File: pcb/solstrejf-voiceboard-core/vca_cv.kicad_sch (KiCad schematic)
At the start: 0 parts

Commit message: Inital draft of the voice board power supplys and core.
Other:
- title: (none) -> VCA Control Voltage Summing Amplifier
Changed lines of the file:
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@@
 	(generator_version "8.0")
 	(paper "A4")
+	(title_block
+		(title "VCA Control Voltage Summing Amplifier")
+		(date "2024-08-24")
+		(rev "1.0")
+	)
 )

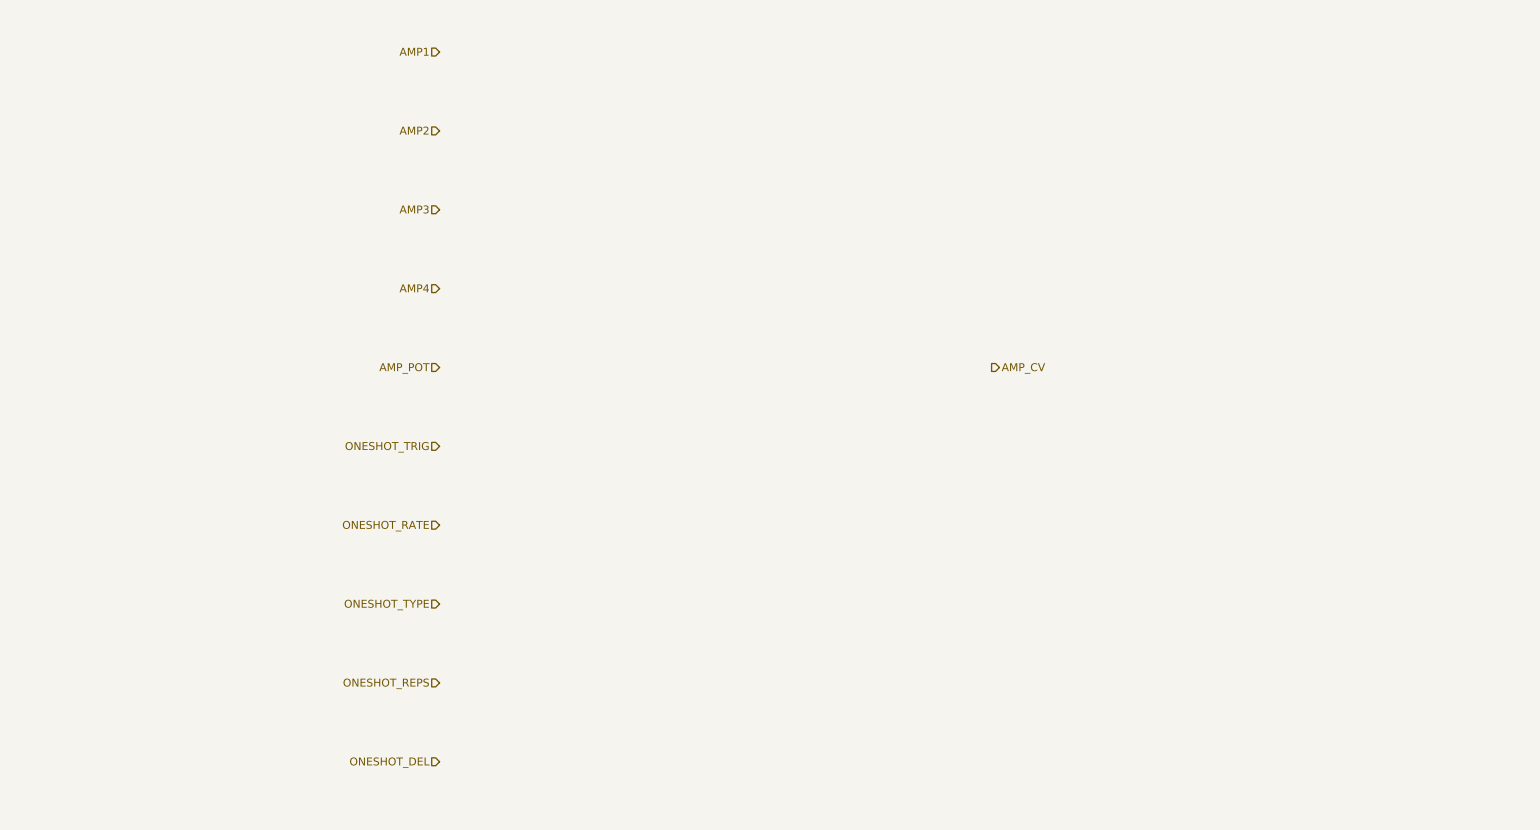
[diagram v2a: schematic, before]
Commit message: created schematic for CV circuits: PAN, VCA, and FREQ. Created a new symbol for the ONESHOT envelope generator
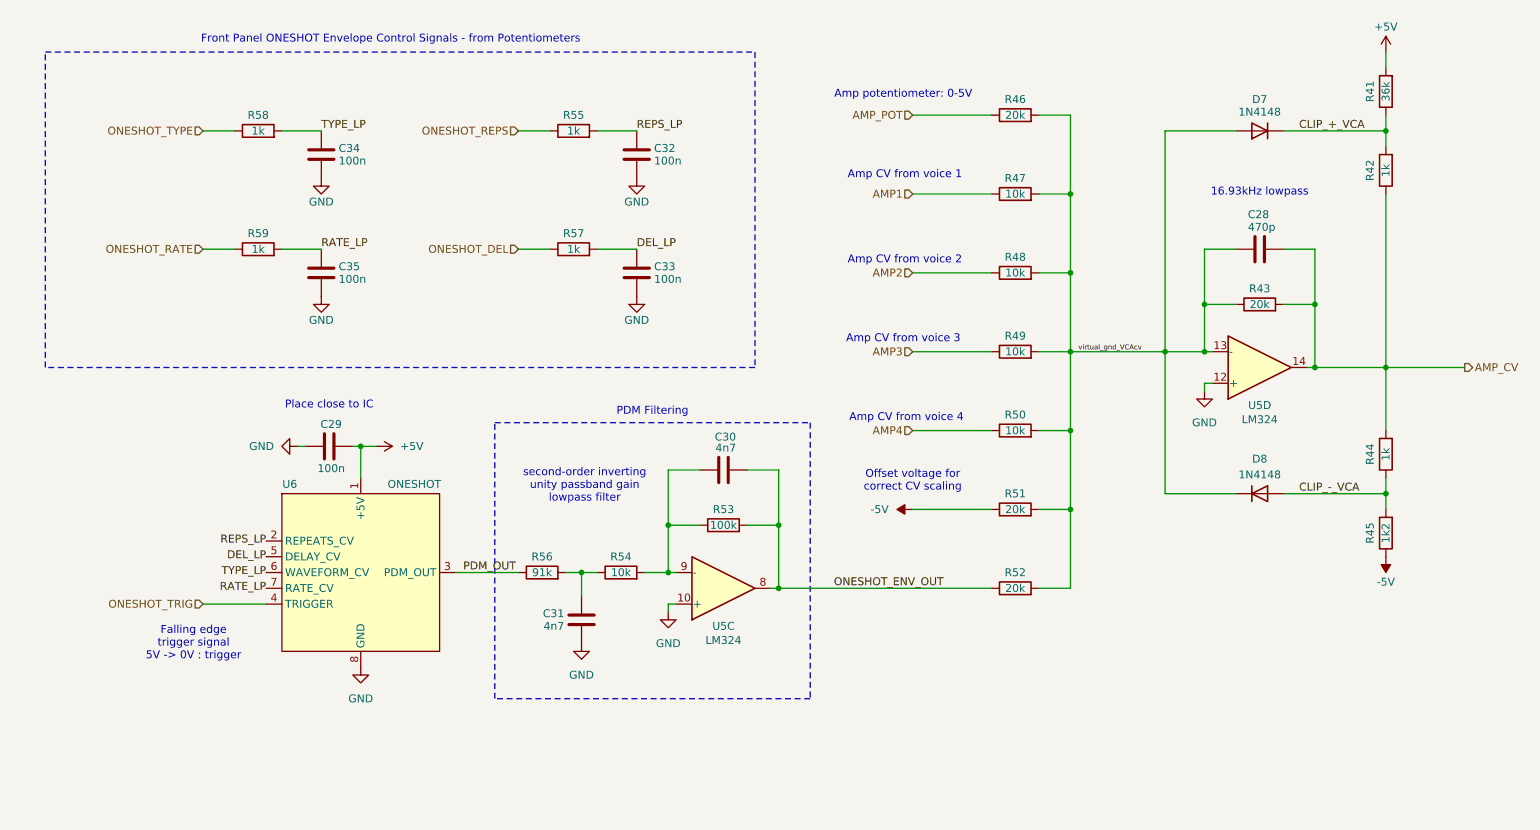
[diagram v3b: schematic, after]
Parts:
- added C28: 470p, Capacitor_THT:C_Disc_D5.0mm_W2.5mm_P5.00mm, symbol Device:C
- added C29, C32, C33, C34, C35: 100n, Capacitor_THT:C_Disc_D5.0mm_W2.5mm_P5.00mm, symbol Device:C
- added C30, C31: 4n7, Capacitor_THT:C_Disc_D5.0mm_W2.5mm_P5.00mm, symbol Device:C
- added D7, D8: 1N4148, Diode_THT:D_DO-35_SOD27_P7.62mm_Horizontal, symbol Diode:1N4148
- added R41: 36k, Resistor_THT:R_Axial_DIN0207_L6.3mm_D2.5mm_P10.16mm_Horizontal, symbol Device:R
- added R42, R44, R55, R57, R58, R59: 1k, Resistor_THT:R_Axial_DIN0207_L6.3mm_D2.5mm_P10.16mm_Horizontal, symbol Device:R
- added R43, R46, R51, R52: 20k, Resistor_THT:R_Axial_DIN0207_L6.3mm_D2.5mm_P10.16mm_Horizontal, symbol Device:R
- added R45: 1k2, Resistor_THT:R_Axial_DIN0207_L6.3mm_D2.5mm_P10.16mm_Horizontal, symbol Device:R
- added R47, R48, R49, R50, R54: 10k, Resistor_THT:R_Axial_DIN0207_L6.3mm_D2.5mm_P10.16mm_Horizontal, symbol Device:R
- added R53: 100k, Resistor_THT:R_Axial_DIN0207_L6.3mm_D2.5mm_P10.16mm_Horizontal, symbol Device:R
- added R56: 91k, Resistor_THT:R_Axial_DIN0207_L6.3mm_D2.5mm_P10.16mm_Horizontal, symbol Device:R
- added U5: LM324, Package_DIP:DIP-14_W7.62mm, symbol Amplifier_Operational:LM324
- added U6: ONESHOT, Package_DIP:DIP-8_W7.62mm_Socket, symbol Kromftronics_Custom:ONSHOT
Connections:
- net AMP1: now also R47.1
- net AMP2: now also R48.1
- net AMP3: now also R49.1
- net AMP4: now also R50.1
- net AMP_CV: now also C28.2, R42.1, R43.2, R44.2, U5.14
- net AMP_POT: now also R46.1
- net ONESHOT_DEL: now also R57.1
- net ONESHOT_RATE: now also R59.1
- net ONESHOT_REPS: now also R55.1
- net ONESHOT_TRIG: now also U6.4 (TRIGGER)
- net ONESHOT_TYPE: now also R58.1
- new net: C31.2, R54.1, R56.2
- new net: C30.1, R53.1, R54.2, U5.9 (-)
- new net +5V: C29.2, R41.2, U6.1 (+5V)
- new net -5V: R45.1, R51.1
- new net CLIP_+_VCA: D7.1 (K), R41.1, R42.2
- new net CLIP_-_VCA: D8.2 (A), R44.1, R45.2
- new net DEL_LP: C33.2, R57.2, U6.5 (DELAY_CV)
- new net GND: C29.1, C31.1, C32.1, C33.1, C34.1, C35.1, U5.10 (+), U5.12 (+), U6.8 (GND)
- new net ONESHOT_ENV_OUT: C30.2, R52.1, R53.2, U5.8
- new net PDM_OUT: R56.1, U6.3 (PDM_OUT)
- new net RATE_LP: C35.2, R59.2, U6.7 (RATE_CV)
- new net REPS_LP: C32.2, R55.2, U6.2 (REPEATS_CV)
- new net TYPE_LP: C34.2, R58.2, U6.6 (WAVEFORM_CV)
- new net virtual_gnd_VCAcv: C28.1, D7.2 (A), D8.1 (K), R43.1, R46.2, R47.2, R48.2, R49.2, R50.2, R51.2, R52.2, U5.13 (-)
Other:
- note added: "16.93kHz lowpass"
- note added: "Amp CV from voice 1"
- note added: "Amp CV from voice 2"
- note added: "Amp CV from voice 3"
- note added: "Amp CV from voice 4"
- note added: "Amp potentiometer: 0-5V"
- note added: "Falling edge trigger signal 5V -> 0V : trigger"
- note added: "Front Panel ONESHOT Envelope Control Signals - from Potentiometers"
- note added: "Offset voltage for correct CV scaling"
- note added: "PDM Filtering"
- note added: "Place close to IC"
- note added: "second-order inverting unity passband gain lowpass filter"

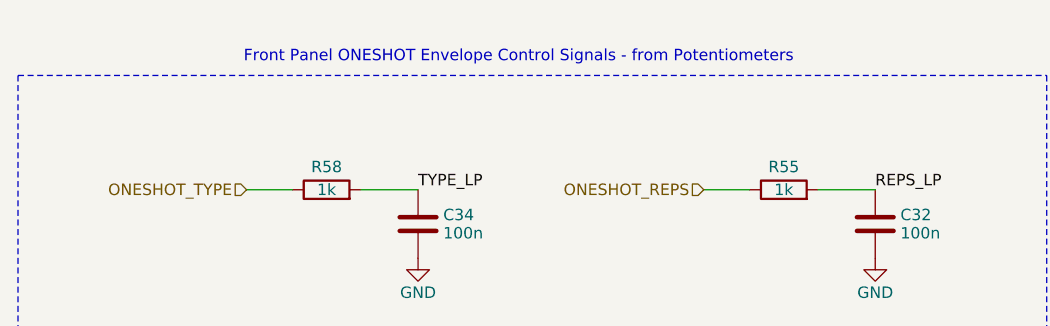
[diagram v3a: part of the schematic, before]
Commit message: created voice board front panel KiCad projects. Made some updates in the Kromftronics KiCad repo.
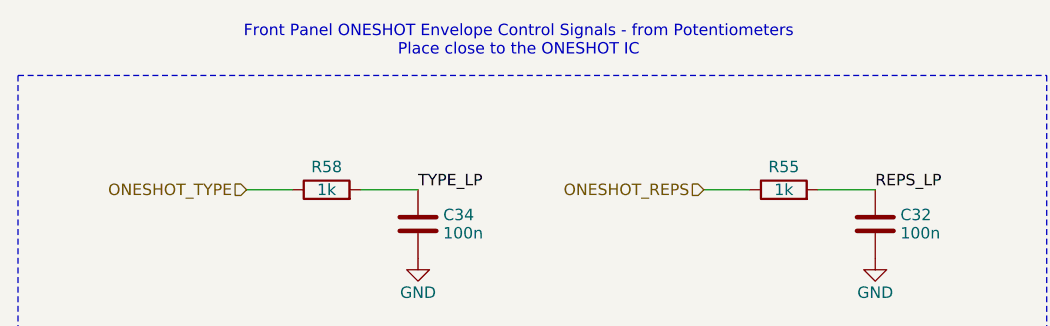
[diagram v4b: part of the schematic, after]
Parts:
- U6: symbol Kromftronics_Custom:ONSHOT -> Kromftronics_Custom:ONESHOT
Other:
- note added: "Front Panel ONESHOT Envelope Control Signals - from Potentiometers Place close to the ONESHOT IC"
- note removed: "Front Panel ONESHOT Envelope Control Signals - from Potentiometers"
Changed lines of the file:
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@@
 		)
 	)
-	(text "Front Panel ONESHOT Envelope Control Signals - from Potentiometers"
+	(text "Front Panel ONESHOT Envelope Control Signals - from Potentiometers\nPlace close to the ONESHOT IC"
 		(exclude_from_sim no)
 		(at 81.026 48.768 0)
@@
 				(size 1.27 1.27)
 			)
+			(justify bottom)
 		)
 	)
@@
 	)
 	(symbol
-		(lib_id "Kromftronics_Custom:ONSHOT")
+		(lib_id "Kromftronics_Custom:ONESHOT")
 		(at 76.2 147.32 0)
 		(unit 1)

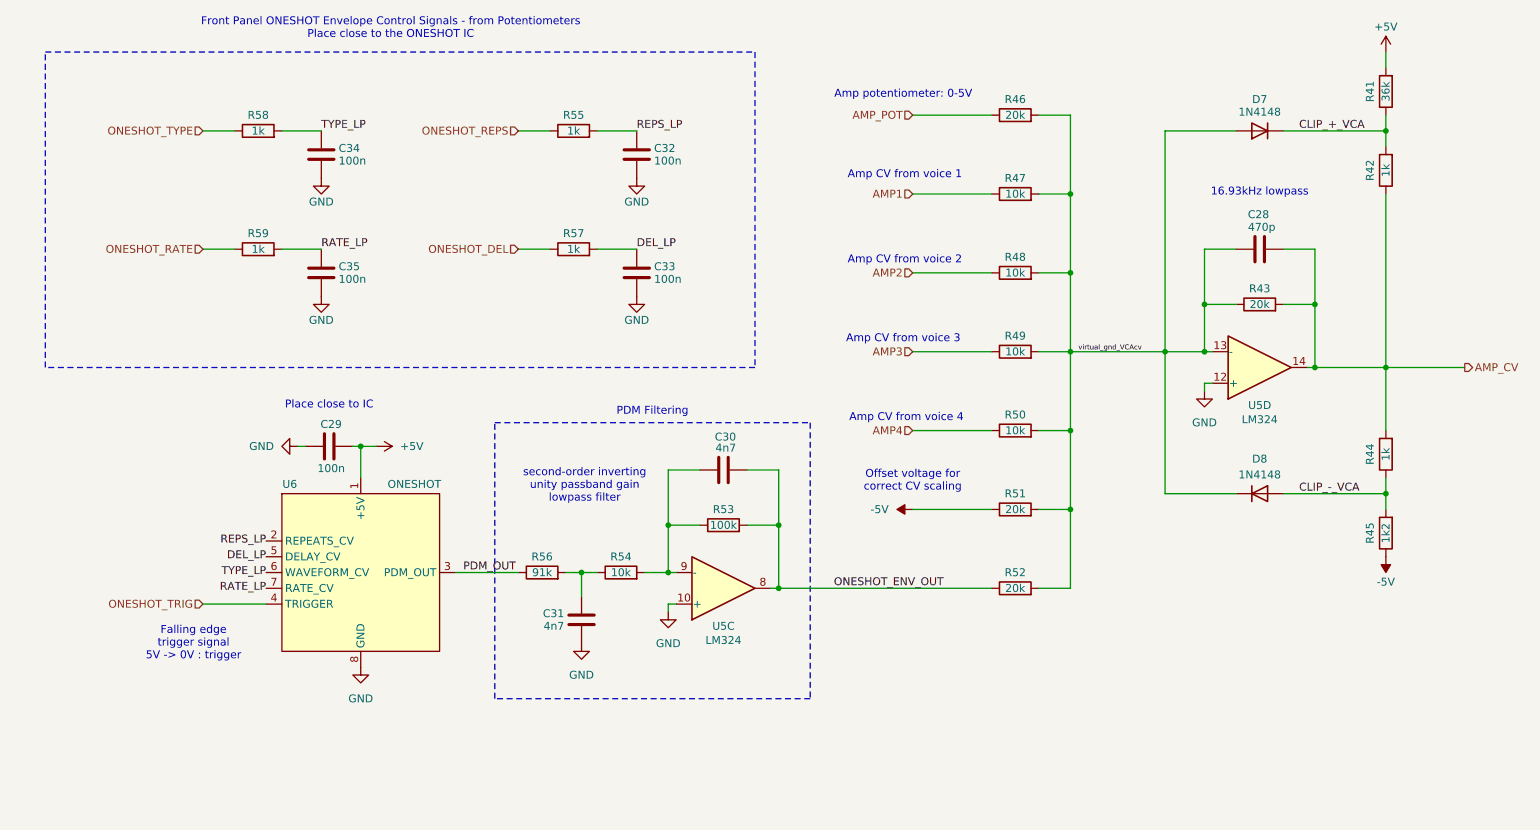
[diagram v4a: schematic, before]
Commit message: updated Kromftronics submodule name and edited path in all PCB projects. Added work-in-progress for the front-panel PCB and the small updates in the voice-board schematic
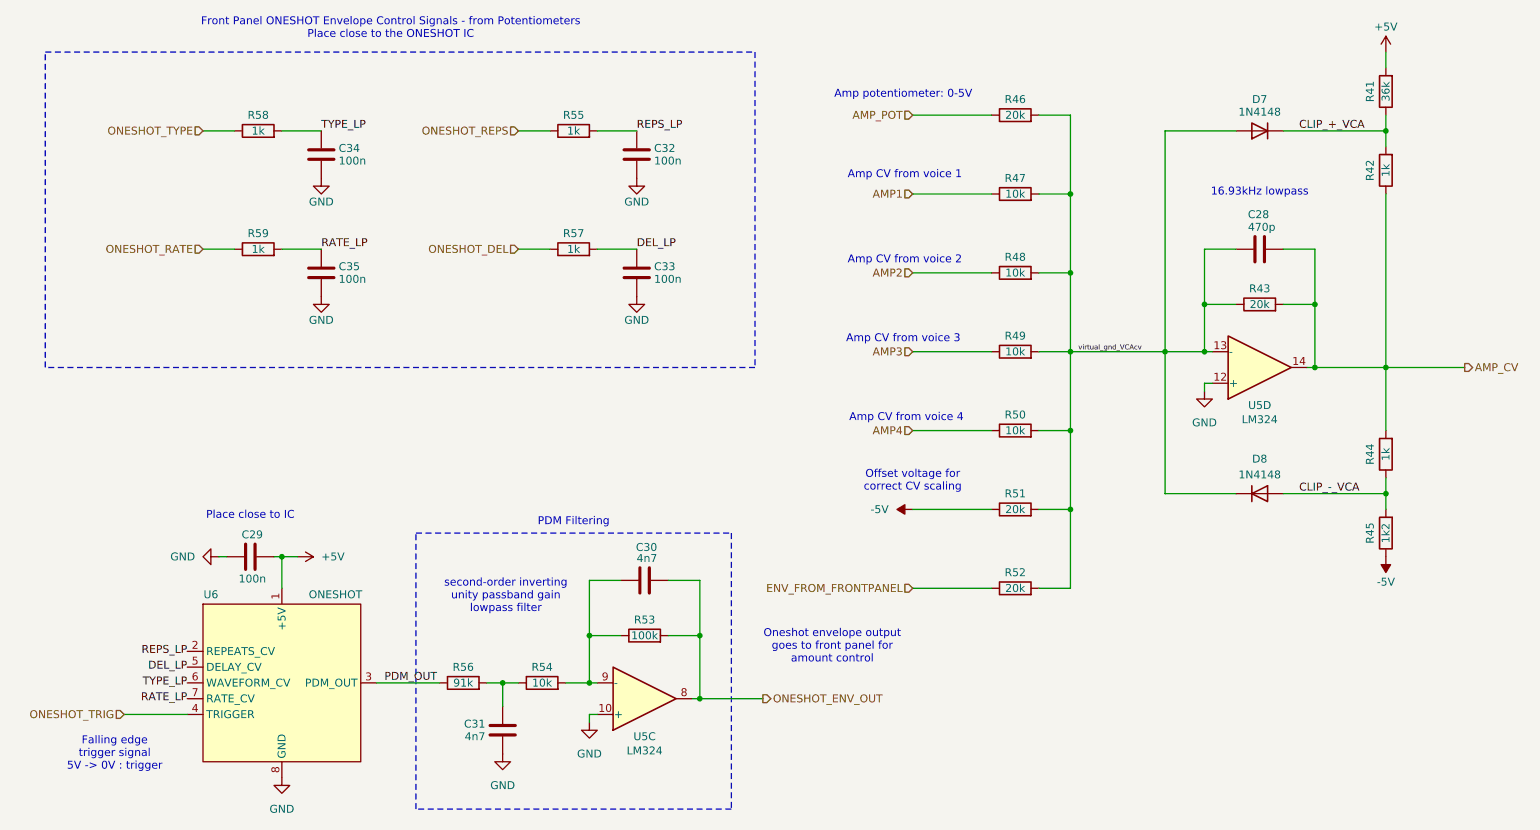
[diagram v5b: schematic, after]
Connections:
- net ONESHOT_ENV_OUT: no longer R52.1
- new net ENV_FROM_FRONTPANEL: R52.1
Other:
- note added: "Oneshot envelope output goes to front panel for amount control"
- moved on the sheet: C29, C30, C31, R53, R54, R56, U5C, U6
